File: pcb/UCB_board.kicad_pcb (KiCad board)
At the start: 4 copper layers, 160 x 100 mm, 174 parts, among them IC1 SN65HVD75DR, J1 DIN41612_02x32_AC, J2 TC2030, J3 Conn_01x02_Pin, T1 H1102NL, U1 W5500, U2 LM4040DBZ-3, U3 USBLC6-2SC6, U4 USBLC6-2SC6, U5 USBLC6-2SC6, U6 FM24C64B, U7 STM32H563VITx, Y1 3225-25M-SR, Y2 3225-25M-SR, Y3 Si5351C-B-GM, Y4 3225-25M-SR

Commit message: New routing
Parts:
- removed H1, H2: MountingHole, MountingHole:MountingHole_2.7mm_M2.5
- added C67: 10u, Capacitor_SMD:C_1206_3216Metric_Pad1.33x1.80mm_HandSolder, F.Cu at (183.6, 32.7)
- added C68: 100n, Capacitor_SMD:C_0603_1608Metric_Pad1.08x0.95mm_HandSolder, F.Cu at (188.8, 36.5)
- added C69: 100n, Capacitor_SMD:C_0603_1608Metric_Pad1.08x0.95mm_HandSolder, F.Cu at (188.8, 39.0)
- added C70: 100n, Capacitor_SMD:C_0603_1608Metric_Pad1.08x0.95mm_HandSolder, F.Cu at (188.8, 41.5)
- added C71: 100n, Capacitor_SMD:C_0603_1608Metric_Pad1.08x0.95mm_HandSolder, F.Cu at (188.8, 44.0)
- added C72: 10u, Capacitor_SMD:C_1206_3216Metric_Pad1.33x1.80mm_HandSolder, F.Cu at (183.6, 36.0)
- added D18: D_TVS, Diode_SMD:D_MiniMELF, F.Cu at (183.8, 29.3)
- added D19: ?, Diode_SMD:D_SMF, F.Cu at (183.5, 42.7)
- added F4: Polyfuse, Fuse:Fuse_1206_3216Metric_Pad1.42x1.75mm_HandSolder, F.Cu at (200.2, 39.7)
- added L4: LQH32PN101MN0L, Inductor_SMD:L_1210_3225Metric, F.Cu at (194.0, 36.2)
- moved TP22 6.53 mm to (208.8, 66.9)
- moved X1 1.25 mm to (173.4, 100.0)
- moved R24 0.29 mm to (201.3, 89.1), turned to 135 degrees
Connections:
- X1 pad 11: /UniConnector/CLK_IN1 -> /UniConnector/CLK_IN2
- X1 pad 13: GND -> /UniConnector/CLK_IN1
- X1 pad 15: /MCU/IO_1 -> GND
- X1 pad 16: /MCU/IO_2 -> GND
- X1 pad 17: /MCU/IO_3 -> /MCU/IO_1
- X1 pad 18: /MCU/IO_4 -> /MCU/IO_2
- X1 pad 19: /MCU/IO_5 -> /MCU/IO_3
- X1 pad 20: /MCU/IO_6 -> /MCU/IO_4
- X1 pad 21: /MCU/IO_7 -> /MCU/IO_5
- X1 pad 22: /MCU/IO_8 -> /MCU/IO_6
- X1 pad 23: /MCU/IO_9 -> /MCU/IO_7
- X1 pad 24: /MCU/IO_10 -> /MCU/IO_8
- X1 pad 25: /MCU/IO_11 -> /MCU/IO_9
- X1 pad 26: /MCU/IO_12 -> /MCU/IO_10
- X1 pad 27: /MCU/IO_13 -> /MCU/IO_11
- X1 pad 28: /MCU/IO_14 -> /MCU/IO_12
- X1 pad 29: /MCU/IO_15 -> /MCU/IO_13
- X1 pad 30: /MCU/IO_16 -> /MCU/IO_14
- X1 pad 31: /MCU/IO_17 -> /MCU/IO_15
- X1 pad 32: /MCU/IO_18 -> /MCU/IO_16
- X1 pad 33: /MCU/IO_19 -> /MCU/IO_17
- X1 pad 34: /MCU/IO_20 -> /MCU/IO_18
- X1 pad 35: /MCU/IO_21 -> /MCU/IO_19
- X1 pad 36: /MCU/IO_22 -> /MCU/IO_20
- X1 pad 37: /MCU/IO_23 -> /MCU/IO_21
- X1 pad 38: /MCU/IO_24 -> /MCU/IO_22
- X1 pad 39: /MCU/IO_25 -> /MCU/IO_23
- X1 pad 40: /MCU/IO_26 -> /MCU/IO_24
- X1 pad 41: /MCU/IO_27 -> /MCU/IO_25
- X1 pad 42: /MCU/IO_28 -> /MCU/IO_26
- X1 pad 43: /MCU/IO_29 -> /MCU/IO_27
- X1 pad 44: /MCU/IO_30 -> /MCU/IO_28
- X1 pad 45: /MCU/IO_31 -> /MCU/IO_29
- X1 pad 46: /MCU/IO_32 -> /MCU/IO_30
- X1 pad 47: /MCU/IO_33 -> /MCU/IO_31
- X1 pad 48: /MCU/IO_34 -> /MCU/IO_32
- X1 pad 49: /MCU/IO_35 -> /MCU/IO_33
- X1 pad 50: /MCU/IO_36 -> /MCU/IO_34
- X1 pad 51: /MCU/IO_37 -> /MCU/IO_35
- X1 pad 52: /MCU/IO_38 -> /MCU/IO_36
- X1 pad 53: /MCU/IO_39 -> /MCU/IO_37
- X1 pad 54: /MCU/IO_40 -> /MCU/IO_38
- X1 pad 55: /MCU/IO_41 -> /MCU/IO_39
- X1 pad 56: /MCU/IO_42 -> /MCU/IO_40
- X1 pad 57: /MCU/IO_43 -> /MCU/IO_41
- X1 pad 58: /MCU/IO_44 -> /MCU/IO_42
- X1 pad 59: /MCU/IO_45 -> /MCU/IO_43
- X1 pad 60: /MCU/IO_46 -> /MCU/IO_44
- X1 pad 61: /MCU/IO_47 -> /MCU/IO_45
- X1 pad 62: /MCU/IO_48 -> /MCU/IO_46
- X1 pad 63: /MCU/IO_49 -> /MCU/IO_47
- X1 pad 64: /MCU/IO_50 -> /MCU/IO_48
- X1 pad 65: /MCU/IO_51 -> /MCU/IO_49
- X1 pad 66: /MCU/IO_52 -> /MCU/IO_50
- X1 pad 67: /MCU/IO_53 -> /MCU/IO_51
- X1 pad 68: /MCU/IO_54 -> /MCU/IO_52
- X1 pad 69: /MCU/IO_55 -> /MCU/IO_53
- X1 pad 7: GND -> -12V
- X1 pad 70: /MCU/IO_56 -> /MCU/IO_54
- X1 pad 71: /MCU/IO_57 -> /MCU/IO_55
- X1 pad 72: unconnected-(X1-Pad72) -> /MCU/IO_56
- X1 pad 73: unconnected-(X1-Pad73) -> /MCU/IO_57
- X1 pad 8: GND -> -12V
- X1 pad 9: /UniConnector/CLK_IN2 -> GND
- Y3 pad 4: /MCU/SDA -> /MCU/SCL
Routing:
- net Earth: track 272.2 -> 157.7 mm
- net +5V: track 57.4 -> 149.6 mm, vias 7 -> 10
- net /MCU/SDA: track 32.0 -> 51.1 mm, vias 2 -> 3
- net /MCU/SCL: track 31.9 -> 49.6 mm, vias 2 -> 3
- net GND: track 92.5 -> 102.3 mm, vias 35 -> 43
- net +3.3V: track 261.4 -> 268.6 mm, vias 35 -> 37
- net /MCU/IO_16: track 42.0 -> 38.4 mm, vias 3 -> 2
- net /UniConnector/CLK_IN1: track 27.8 -> 24.6 mm
- net unconnected-(X1-Pad72): track 2.59 -> 0.00 mm, vias 1 -> 0
- net unconnected-(X1-Pad73): track 2.58 -> 0.00 mm, vias 1 -> 0
- net +12V: track 38.2 -> 35.7 mm, vias 6 -> 8
- net /MCU/IO_17: track 40.5 -> 38.3 mm
- net /MCU/IO_5: track 44.3 -> 42.0 mm
- net /MCU/IO_23: track 39.5 -> 37.3 mm
- net /MCU/IO_46: track 30.5 -> 32.7 mm
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- added copper zone on In2.Cu, net /ConnectorDIN41612/PSU/+12V_IN
- added copper zone on In2.Cu, net /ConnectorDIN41612/PSU/+3,3V_IN
- added copper zone on In2.Cu, net /ConnectorDIN41612/PSU/+5V_IN
- removed copper zone on In1.Cu, net /ConnectorDIN41612/PSU/+12V_IN
- removed copper zone on In1.Cu, net /ConnectorDIN41612/PSU/+3,3V_IN
- removed copper zone on In1.Cu, net /ConnectorDIN41612/PSU/+5V_IN
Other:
- board size 160 x 100 mm -> 56.8 x 100 mm

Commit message: More routing
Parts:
- D18, D19, F4: moved to B.Cu
- moved D18 32.8 mm to (186.5, 62.1)
- moved L4 28.1 mm to (186.2, 63.2), turned to 90 degrees
- moved C72 27.4 mm to (183.4, 63.4), turned to 90 degrees
- moved C67 25.7 mm to (184.1, 58.3), turned to 90 degrees
- moved C71 23.2 mm to (188.6, 67.2), turned to -90 degrees
- moved C68 22.4 mm to (188.1, 58.9), turned to 90 degrees
- moved C70 22.3 mm to (188.6, 63.8), turned to 90 degrees
- moved F4 22.1 mm to (188.3, 58.3), turned to 90 degrees
- moved C69 19.9 mm to (189.6, 58.9), turned to 90 degrees
- moved D19 15.7 mm to (184.1, 58.4), turned to 90 degrees
- moved TP22 8.43 mm to (215.5, 72.1)
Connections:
- X1 pad 74: unconnected-(X1-Pad74) -> GND
- X1 pad 75: unconnected-(X1-Pad75) -> GND
- X1 pad 76: unconnected-(X1-Pad76) -> GND
- X1 pad 77: unconnected-(X1-Pad77) -> GND
- X1 pad 78: unconnected-(X1-Pad78) -> GND
- X1 pad 79: unconnected-(X1-Pad79) -> GND
- X1 pad 80: unconnected-(X1-Pad80) -> GND
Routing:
- net /ConnectorDIN41612/PSU/-12V_IN: track 5.08 -> 43.4 mm, vias 0 -> 5
- net -12V: track 0.01 -> 19.5 mm, vias 0 -> 4
- net GND: track 102.3 -> 111.7 mm, vias 43 -> 46
- net unconnected-(X1-Pad80): track 2.59 -> 0.00 mm, vias 1 -> 0
- net unconnected-(X1-Pad78): track 2.59 -> 0.00 mm, vias 1 -> 0
- net unconnected-(X1-Pad76): track 2.59 -> 0.00 mm, vias 1 -> 0
- net unconnected-(X1-Pad74): track 2.59 -> 0.00 mm, vias 1 -> 0
- net unconnected-(X1-Pad79): track 2.58 -> 0.00 mm, vias 1 -> 0
- net unconnected-(X1-Pad77): track 2.58 -> 0.00 mm, vias 1 -> 0
- net unconnected-(X1-Pad75): track 2.58 -> 0.00 mm, vias 1 -> 0
- net /ConnectorDIN41612/PSU/+12V_IN: track 36.4 -> 35.9 mm
- net Net-(D18-A2): vias 0 -> 5
- added copper zone on F.Cu, net -12V
- added copper zone on B.Cu, net /ConnectorDIN41612/PSU/-12V_IN
- added copper zone on In2.Cu, net /ConnectorDIN41612/PSU/-12V_IN
- added copper zone on B.Cu, net Net-(D18-A2)
- added copper zone on F.Cu, net Net-(D18-A2)

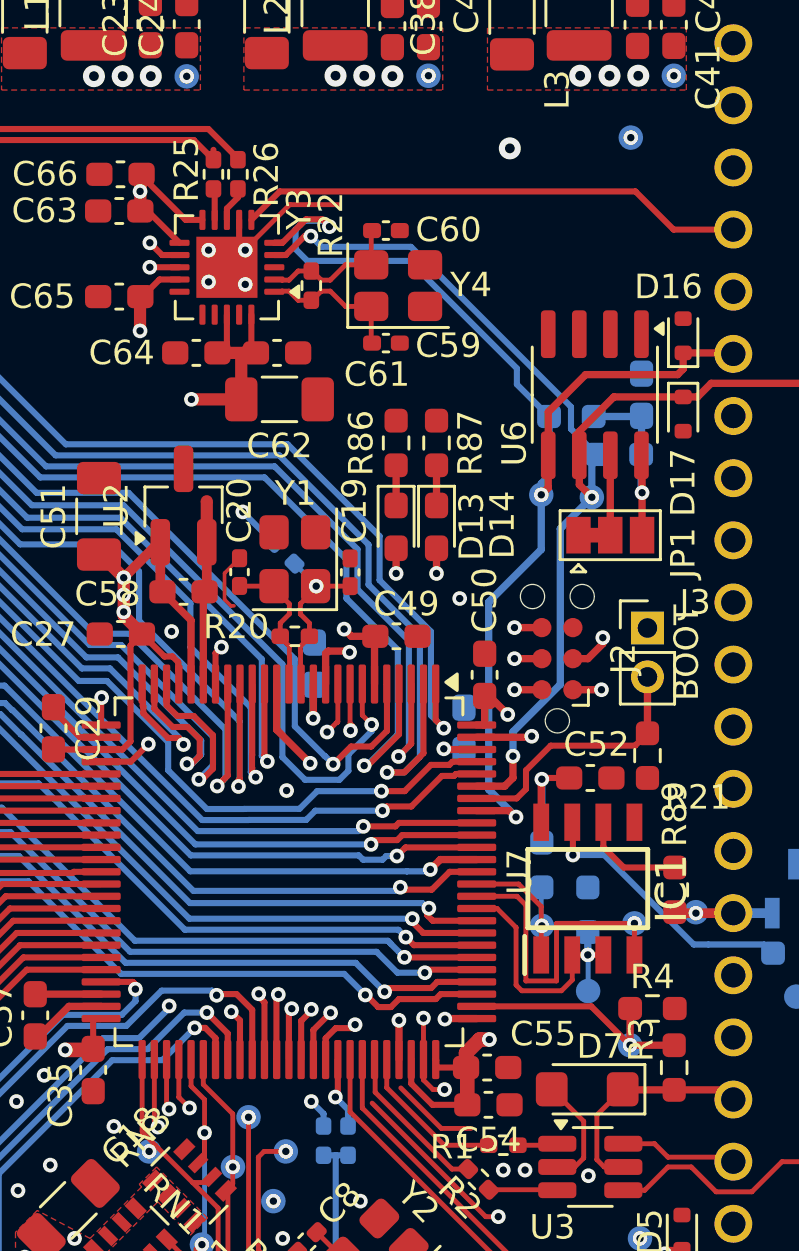
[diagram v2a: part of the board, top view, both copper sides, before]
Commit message: More routing ...
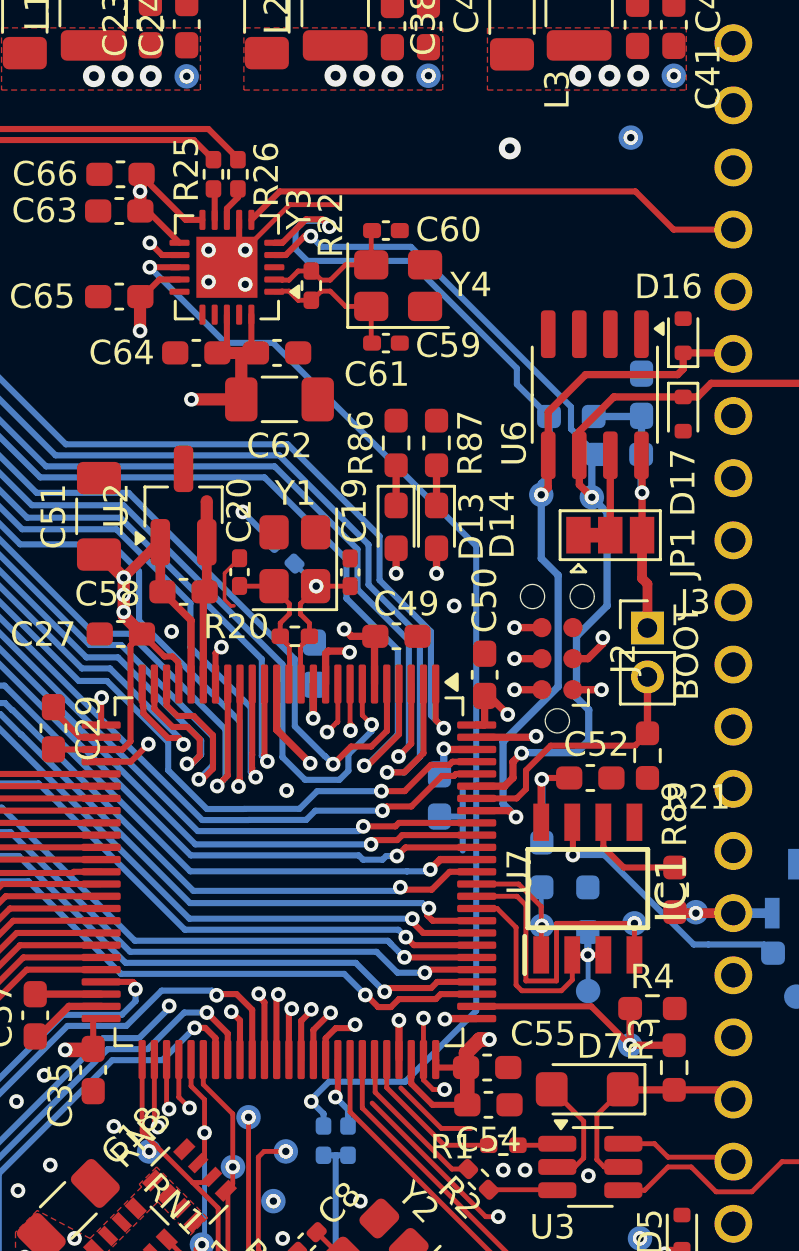
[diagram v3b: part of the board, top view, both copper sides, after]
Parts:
- moved C56 2.90 mm to (207.6, 99.0), turned to 90 degrees
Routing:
- net /Clock/CLK0: track 41.3 -> 47.8 mm
- net +3.3V: track 268.6 -> 272.4 mm
- net GND: track 111.7 -> 115.4 mm
- net /MCU/SCL: track 49.6 -> 51.8 mm
